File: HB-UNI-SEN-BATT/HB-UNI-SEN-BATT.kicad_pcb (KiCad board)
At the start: 2 copper layers, 75 x 75 mm, 25 parts, among them J0 BATT, J1 I2C_1, J2 I2C_2, J3 A0, J4 A1, J5 A2, J6 A3, J7 PROG, SW1 CONFIG_BUTTON, U1 ArduinoProMini, U2 CC1101

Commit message: Optimized footprints
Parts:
- moved BT1 0.37 mm to (173.0, 142.0)
- moved BT2 0.17 mm to (104.0, 85.0)
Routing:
- net Net-(BT1-Pad2): track 52.8 -> 53.9 mm
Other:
- board text added: "A3"
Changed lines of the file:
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@@
     (thickness 1.6)
     (drawings 65)
-    (tracks 199)
+    (tracks 196)
     (zones 0)
     (modules 25)
@@
   )
   (module Homebrew:BATTERY_HOLDER_GOOBAY_AA (layer F.Cu)
-    (at 172.72 142.24 90)
-    (fp_text reference BT1 (at 17.78 -8.255 90) (layer F.SilkS) hide
-      (effects (font (size 1 1) (thickness 0.15)))
-    )
-    (fp_text value AA (at 48.1 -1.5 90) (layer F.Fab)
-      (effects (font (size 1 1) (thickness 0.15)))
-    )
-    (fp_text user + (at 51.1 -8.7 90) (layer F.SilkS)
-      (effects (font (size 3 3) (thickness 0.5)))
-    )
-    (fp_circle (center 51.1 -8.5) (end 52.6 -7) (layer F.SilkS) (width 0.15))
-    (fp_circle (center 6.8 -8.5) (end 8.3 -7) (layer F.SilkS) (width 0.15))
-    (fp_text user - (at 6.8 -8.7 90) (layer F.SilkS)
-      (effects (font (size 3 3) (thickness 0.5)))
-    )
-    (fp_line (start 0 0) (end 0 -17) (layer F.SilkS) (width 0.15))
-    (fp_line (start 0 -17) (end 57 -17) (layer F.SilkS) (width 0.15))
-    (fp_line (start 57 -17) (end 57 0) (layer F.SilkS) (width 0.15))
-    (fp_line (start 57 0) (end 0 0) (layer F.SilkS) (width 0.15))
-    (pad 2 thru_hole circle (at 2.8 -8.5 90) (size 1.6 1.6) (drill 0.8) (layers *.Cu *.Mask)
-      (net 23 "Net-(BT1-Pad2)"))
-    (pad 1 thru_hole circle (at 55.1 -8.5 90) (size 1.6 1.6) (drill 0.8) (layers *.Cu *.Mask)
-      (net 1 +3V3))
-    (pad "" np_thru_hole circle (at 28.5 -8.5 90) (size 2.9 2.9) (drill 2.9) (layers *.Cu *.Mask))
-  )
-  (module Homebrew:BATTERY_HOLDER_GOOBAY_AA (layer F.Cu)
-    (at 104.14 85.09 270)
+    (at 104 85 270)
     (fp_text reference BT2 (at 18.415 -8.89 270) (layer F.SilkS) hide
       (effects (font (size 1 1) (thickness 0.15)))
@@
     (pad 1 thru_hole circle (at 1.166726 -1.166726) (size 0.7 0.7) (drill 0.4) (layers *.Cu *.Mask))
   )
+  (module Homebrew:BATTERY_HOLDER_GOOBAY_AA (layer F.Cu)
+    (at 173 142 90)
+    (fp_text reference BT1 (at 17.78 -8.255 90) (layer F.SilkS) hide
+      (effects (font (size 1 1) (thickness 0.15)))
+    )
+    (fp_text value AA (at 48.1 -1.5 90) (layer F.Fab)
+      (effects (font (size 1 1) (thickness 0.15)))
+    )
+    (fp_text user + (at 51.1 -8.7 90) (layer F.SilkS)
+      (effects (font (size 3 3) (thickness 0.5)))
+    )
+    (fp_circle (center 51.1 -8.5) (end 52.6 -7) (layer F.SilkS) (width 0.15))
+    (fp_circle (center 6.8 -8.5) (end 8.3 -7) (layer F.SilkS) (width 0.15))
+    (fp_text user - (at 6.8 -8.7 90) (layer F.SilkS)
+      (effects (font (size 3 3) (thickness 0.5)))
+    )
+    (fp_line (start 0 0) (end 0 -17) (layer F.SilkS) (width 0.15))
+    (fp_line (start 0 -17) (end 57 -17) (layer F.SilkS) (width 0.15))
+    (fp_line (start 57 -17) (end 57 0) (layer F.SilkS) (width 0.15))
+    (fp_line (start 57 0) (end 0 0) (layer F.SilkS) (width 0.15))
+    (pad 2 thru_hole circle (at 1.9 -8.5 90) (size 1.6 1.6) (drill 0.8) (layers *.Cu *.Mask)
+      (net 23 "Net-(BT1-Pad2)"))
+    (pad 1 thru_hole circle (at 55.1 -8.5 90) (size 1.6 1.6) (drill 0.8) (layers *.Cu *.Mask)
+      (net 1 +3V3))
+    (pad "" np_thru_hole circle (at 28.5 -8.5 90) (size 2.9 2.9) (drill 2.9) (layers *.Cu *.Mask))
+  )
   (gr_text "(c) Alexander Reinert" (at 112.395 90.17 90) (layer B.SilkS)
     (effects (font (size 1.2 1.2) (thickness 0.2)) (justify left mirror))
@@
     (effects (font (size 0.8 0.8) (thickness 0.15) italic))
   )
-  (gr_text A1 (at 151.13 96.52) (layer F.SilkS)
+  (gr_text A3 (at 151.13 96.52) (layer F.SilkS)
     (effects (font (size 0.8 0.8) (thickness 0.15) italic))
   )
@@
   (gr_arc (start 169 146) (end 176 146) (angle 90) (layer Edge.Cuts) (width 0.15))
   (gr_arc (start 108 85) (end 101 85) (angle 90) (layer Edge.Cuts) (width 0.15))
+  (segment (start 164.5 86.9) (end 160.115 86.9) (width 0.35) (layer F.Cu) (net 1))
+  (segment (start 156.21 90.805) (end 158.75 88.265) (width 0.35) (layer F.Cu) (net 1))
+  (segment (start 154.94 92.075) (end 156.21 90.805) (width 0.35) (layer F.Cu) (net 1))
+  (segment (start 160.115 86.9) (end 158.75 88.265) (width 0.35) (layer F.Cu) (net 1))
   (segment (start 142.28 129.945) (end 143.28 129.945) (width 0.35) (layer F.Cu) (net 1))
   (segment (start 142.28 129.945) (end 147.09 129.945) (width 0.35) (layer F.Cu) (net 1))
@@
   (segment (start 154.94 92.075) (end 153.035 90.17) (width 0.35) (layer F.Cu) (net 1))
   (segment (start 154.94 121.285) (end 154.94 92.075) (width 0.35) (layer F.Cu) (net 1))
-  (segment (start 154.94 92.075) (end 156.21 90.805) (width 0.35) (layer F.Cu) (net 1))
   (segment (start 154.94 130.81) (end 154.94 121.285) (width 0.35) (layer F.Cu) (net 1))
   (segment (start 154.94 121.285) (end 154.94 120.65) (width 0.35) (layer F.Cu) (net 1))
-  (segment (start 158.75 88.265) (end 160.02 86.995) (width 0.35) (layer F.Cu) (net 1))
-  (segment (start 156.21 90.805) (end 158.75 88.265) (width 0.35) (layer F.Cu) (net 1))
-  (segment (start 160.02 86.995) (end 164.075 86.995) (width 0.35) (layer F.Cu) (net 1))
-  (segment (start 164.075 86.995) (end 164.22 87.14) (width 0.35) (layer F.Cu) (net 1))
   (segment (start 148.59 131.445) (end 153.035 131.445) (width 0.35) (layer F.Cu) (net 1))
   (segment (start 153.035 131.445) (end 153.67 132.08) (width 0.35) (layer F.Cu) (net 1))
@@
   (segment (start 154.535 131.215) (end 153.67 132.08) (width 0.35) (layer F.Cu) (net 1))
   (segment (start 154.535 131.215) (end 154.94 130.81) (width 0.35) (layer F.Cu) (net 1))
-  (segment (start 164.075 86.995) (end 164.22 87.14) (width 0.35) (layer F.Cu) (net 1))
   (segment (start 140.97 90.17) (end 153.035 90.17) (width 0.35) (layer F.Cu) (net 1))
   (segment (start 151.13 148.59) (end 153.67 148.59) (width 0.35) (layer F.Cu) (net 1))
@@
   (segment (start 140.97 111.76) (end 140.97 112.395) (width 0.25) (layer F.Cu) (net 11))
   (segment (start 148.2725 117.7925) (end 147.955 118.11) (width 0.25) (layer F.Cu) (net 12))
-  (segment (start 147.955 118.11) (end 142.445 118.11) (width 0.25) (layer F.Cu) (net 12) (status 800000))
-  (segment (start 142.445 118.11) (end 142.28 117.945) (width 0.25) (layer F.Cu) (net 12) (status C00000))
+  (segment (start 147.955 118.11) (end 142.445 118.11) (width 0.25) (layer F.Cu) (net 12))
+  (segment (start 142.445 118.11) (end 142.28 117.945) (width 0.25) (layer F.Cu) (net 12))
   (segment (start 153.035 113.03) (end 153.035 111.76) (width 0.25) (layer F.Cu) (net 12))
   (segment (start 148.2725 117.7925) (end 153.035 113.03) (width 0.25) (layer F.Cu) (net 12))
@@
   (segment (start 163.83 85.725) (end 165.1 85.725) (width 0.25) (layer F.Cu) (net 22))
   (segment (start 165.1 85.725) (end 165.735 86.36) (width 0.25) (layer F.Cu) (net 22))
-  (segment (start 112.64 140.19) (end 112.64 140.09) (width 0.35) (layer B.Cu) (net 23))
-  (segment (start 112.64 140.09) (end 114.3 138.43) (width 0.35) (layer B.Cu) (net 23))
-  (segment (start 163.21 138.43) (end 164.22 139.44) (width 0.35) (layer B.Cu) (net 23))
-  (segment (start 114.3 138.43) (end 163.21 138.43) (width 0.35) (layer B.Cu) (net 23))
-  (segment (start 164.22 139.44) (end 164.205 139.44) (width 0.35) (layer B.Cu) (net 23))
+  (segment (start 117.475 137.795) (end 114.805 137.795) (width 0.35) (layer B.Cu) (net 23))
+  (segment (start 114.805 137.795) (end 112.5 140.1) (width 0.35) (layer B.Cu) (net 23))
+  (segment (start 117.475 137.795) (end 162.195 137.795) (width 0.35) (layer B.Cu) (net 23))
+  (segment (start 162.195 137.795) (end 164.5 140.1) (width 0.35) (layer B.Cu) (net 23))
   (segment (start 147.955 126.365) (end 153.035 121.285) (width 0.25) (layer F.Cu) (net 24))
   (segment (start 147.955 85.725) (end 146.05 83.82) (width 0.25) (layer B.Cu) (net 24))

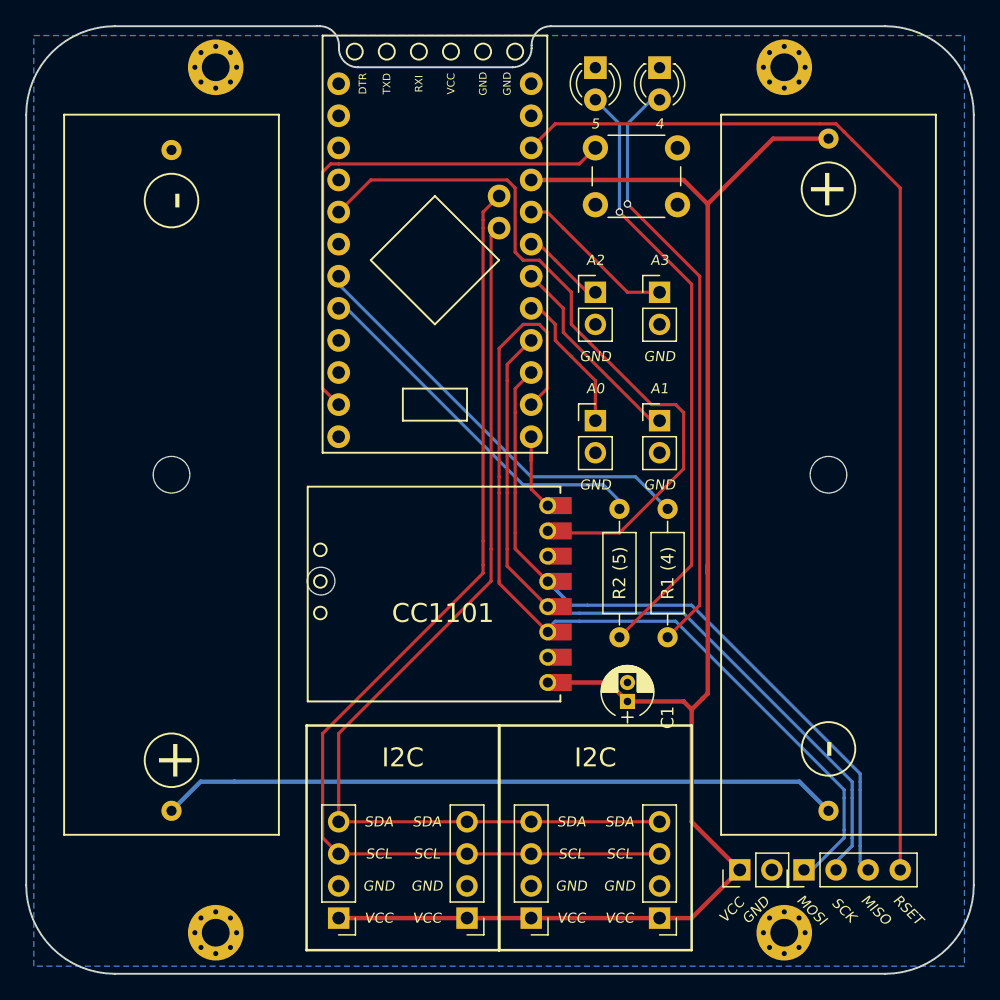
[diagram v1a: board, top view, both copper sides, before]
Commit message: Added reverse polarity protection
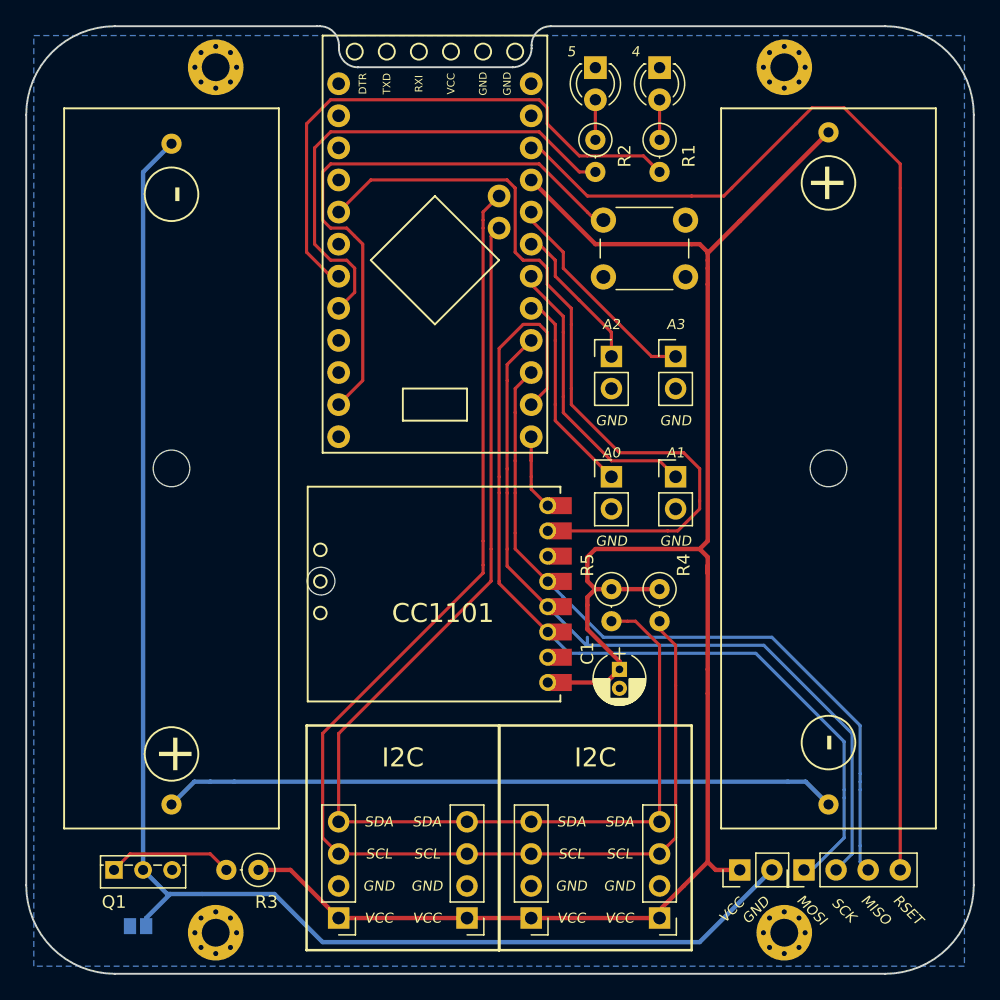
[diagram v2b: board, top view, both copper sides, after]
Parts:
- added J8: NO, Connectors:GS2, B.Cu at (109.9, 149.2)
- added Q1: IRLU024N, TO_SOT_Packages_THT:TO-251_IPAK_Vertical, F.Cu at (108.0, 144.8)
- added R3: 100K, Resistors_THT:R_Axial_DIN0207_L6.3mm_D2.5mm_P2.54mm_Vertical, F.Cu at (119.4, 144.8)
- added R4: 10K, Resistors_THT:R_Axial_DIN0207_L6.3mm_D2.5mm_P2.54mm_Vertical, F.Cu at (151.1, 122.6)
- added R5: 10K, Resistors_THT:R_Axial_DIN0207_L6.3mm_D2.5mm_P2.54mm_Vertical, F.Cu at (147.3, 122.6)
- R1, R2: footprint Resistors_THT:R_Axial_DIN0207_L6.3mm_D2.5mm_P10.16mm_Horizontal -> Resistors_THT:R_Axial_DIN0207_L6.3mm_D2.5mm_P2.54mm_Vertical
- moved R2 39.4 mm to (146.1, 87.0), turned to 270 degrees
- moved R1 39.4 mm to (151.1, 87.0), turned to 270 degrees
- moved SW1 5.75 mm to (146.7, 93.3)
- moved J6 5.24 mm to (152.4, 104.1)
- moved J5 5.24 mm to (147.3, 104.1)
- moved J4 4.62 mm to (152.4, 113.7)
- moved J3 4.62 mm to (147.3, 113.7)
- moved C1 2.62 mm to (148.0, 128.9), turned to 270 degrees
- moved BT1 0.50 mm to (173.0, 141.5)
- moved BT2 0.50 mm to (104.0, 84.5)
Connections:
- BT2 pad 2: GND -> Net-(BT2-Pad2)
- J0 pad 2: GND -> Net-(BT2-Pad2)
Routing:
- net Net-(BT2-Pad2): track 0.00 -> 116.3 mm
- net Net-(D2-Pad2): track 48.1 -> 3.18 mm, vias 1 -> 0
- net Net-(D1-Pad2): track 47.4 -> 3.18 mm, vias 1 -> 0
- net +3V3: track 128.8 -> 153.9 mm
- net /SCL: track 83.8 -> 103.2 mm
- net /SDA: track 78.3 -> 96.9 mm
- net Net-(R1-Pad2): track 34.0 -> 45.3 mm
- net Net-(R2-Pad2): track 29.2 -> 40.0 mm
- net Net-(Q1-Pad1): track 0.00 -> 9.94 mm
- net /A2: track 6.66 -> 13.2 mm
- net /A1: track 16.6 -> 22.8 mm
- net /D2: track 57.8 -> 63.2 mm
- net /RSET: track 86.1 -> 91.4 mm
- net /A0: track 11.4 -> 16.3 mm
- net /A3: track 12.8 -> 17.3 mm
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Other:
- rule trace_min: 0.2 -> 0.25
- board text added: "Version 1.5 - 05/2018"
- board text removed: "R1 (4)"
- board text removed: "R2 (5)"
- board text removed: "Version 1.3 - 04/2018"
